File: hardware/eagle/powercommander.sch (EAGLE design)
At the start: 28 parts, among them IC1 ULN2803SO18-1, IC2 7805TV, IC3 MCP2551DIL8, K1 G5NB, K2 G5NB, K3 G5NB, K4 G5NB, K5 G5NB, K6 G5NB, K7 G5NB, K8 G5NB, X2 3KLEMME, X3 2KLEMME, X4 2KLEMME, X5 2KLEMME, X6 2KLEMME

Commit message: neu verkabelt
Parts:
- removed EXT2: EXT2, pinhead:PINHD-2X13
- added D1, D2, D3, D4, D5, D6, D7, D8: (no value), diode:DIODE-SOD323-W
- added D9: (no value), diode:DIODE-MELF-MLL41
- added EXT2-1-4, EXT2-23-26: (no value), pinhead:PINHD-2X2
- added F2: FUSESH35, fuse:FUSESH35
- IC3: value MCP2551DIL8 -> MCP2551SOIC8; device personal-parts:MCP2551DIL8 -> personal-parts:MCP2551SOIC8
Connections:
- net A2 renamed N$14
- net A4 renamed N$9
- net A6 renamed N$12
- net A8 renamed N$13
- removed net N$12 (its old number): IC1.5C, K41.1
- removed net N$13 (its old number): IC1.4C, K51.1
- removed net N$14 (its old number): IC1.3C, K61.1
- removed net N$16: IC1.1C, K81.1
- removed net N$21: EXT1.7, IC1.1B
- removed net N$9 (its old number): IC1.8C, K11.1
- new net N$22: F2.1, PHASE.2
- new net N$24: D8.A, IC1.1C, K81.4
- new net N$26: D6.A, IC1.3C, K61.4
- new net N$27: D5.A, IC1.4C, K51.4
- new net N$28: D4.A, IC1.5C, K41.4
- net +5V: now also D1.C, D2.C, D3.C, D4.C, D5.C, D6.C, D7.C, D8.C, D9.A, EXT2-23-26.4, K11.1, K21.1, K31.1, K41.1, K51.1, K61.1, K71.1, K81.1; no longer EXT2.26, K11.4, K21.4, K31.4, K41.4, K51.4, K61.4, K71.4, K81.4
- net N$10: now also D2.A, K21.4; no longer K21.1
- net N$11: now also D3.A, K31.4; no longer K31.1
- net N$15: now also D7.A, K71.4; no longer K71.1
- net N$2: now also X2.2; no longer X2.1
- net N$20: now also D1.A, IC1.8C, K11.4; no longer EXT1.9, IC1.2B
- net N$5: now also D9.C
- net N$6: now also X2.1; no longer X2.2
- net NULL: now also PHASE.1; no longer PHASE.2
- net PHASE: now also F2.2; no longer PHASE.1
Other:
- moved on the sheet: K1, K2, K3, K4, K5, K6, K7, K8

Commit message: neue board version mit pwm pins
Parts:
- removed EXT2-23-26: (no value), pinhead:PINHD-2X2
- added EXT2-21-26: (no value), pinhead:PINHD-2X3
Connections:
- removed net N$18 (its old number): EXT1.13, IC1.4B
- removed net N$38: EXT1.16, R3.2
- removed net N$39: EXT1.14, R2.2
- removed net N$40: EXT1.12, R1.2
- new net N$16: EXT1.17, IC1.4B
- new net N$21: EXT1.13, IC1.7B
- new net N$25: EXT1.14, IC1.8B
- new net N$29: EXT1.24, R1.2
- new net N$31: EXT1.18, R3.2
- net +5V: now also EXT2-21-26.6; no longer EXT2-23-26.4
- net N$1: now also EXT1.26, IC1.1B; no longer EXT1.21, IC1.8B
- net N$19: now also EXT1.16, IC1.6B; no longer EXT1.11, IC1.3B
- net N$30: now also EXT1.20, R2.2; no longer EXT1.26, IC1.COM
- net N$7: now also EXT1.22, IC1.2B; no longer EXT1.19, IC1.7B
- net N$8: now also EXT1.21, IC1.3B; no longer EXT1.17, IC1.6B
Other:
- moved on the sheet: EXT1, JP3, R1, R2, R3

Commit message: some fixes..
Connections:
- net GND: now also EXT2-21-26.5
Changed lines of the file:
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@@
 <part name="EXT2-21-26" library="pinhead" deviceset="PINHD-2X3" device=""/>
 <part name="EXT2-1-4" library="pinhead" deviceset="PINHD-2X2" device=""/>
+<part name="GND1" library="supply1" deviceset="GND" device=""/>
 </parts>
 <sheets>
@@
 <instance part="EXT2-21-26" gate="A" x="22.86" y="99.06"/>
 <instance part="EXT2-1-4" gate="A" x="25.4" y="83.82"/>
+<instance part="GND1" gate="1" x="10.16" y="91.44"/>
 </instances>
 <busses>
@@
 <wire x1="78.74" y1="139.7" x2="81.28" y2="139.7" width="0.1524" layer="91"/>
 </segment>
-</net>
+<segment>
+<pinref part="EXT2-21-26" gate="A" pin="5"/>
+<pinref part="GND1" gate="1" pin="GND"/>
+<wire x1="20.32" y1="96.52" x2="10.16" y2="96.52" width="0.1524" layer="91"/>
+<wire x1="10.16" y1="96.52" x2="10.16" y2="93.98" width="0.1524" layer="91"/>
+</segment>
+</net>

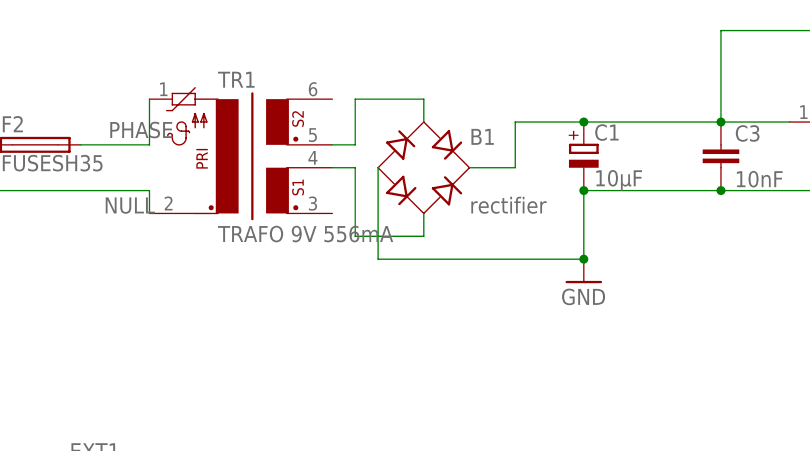
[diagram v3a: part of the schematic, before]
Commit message: removed transformer holes
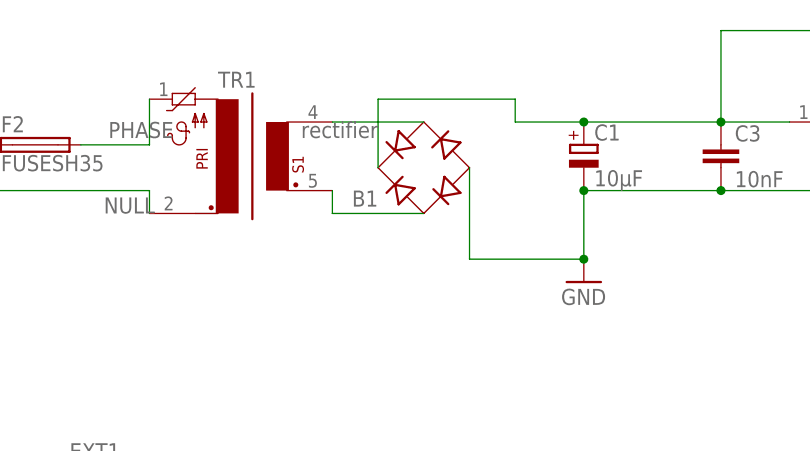
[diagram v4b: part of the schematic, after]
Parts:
- TR1: value TRAFO 9V 556mA -> (none); device trafo:PT04,5-2 -> personal-parts:VC5,0-1
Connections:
- removed net N$3 (its old number): B1.AC1, TR1.5
- new net N$4: B1.AC1, TR1.3
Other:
- moved on the sheet: B1
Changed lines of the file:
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@@
 <part name="IC2" library="linear" deviceset="78*" device="TV" technology="05"/>
 <part name="B1" library="rectifier" deviceset="RB1A" device="" value="rectifier"/>
-<part name="TR1" library="trafo" deviceset="PT04,5-2" device="" value="TRAFO 9V 556mA"/>
 <part name="K1" library="relay-omron-G5NB" deviceset="G5NB" device=""/>
 <part name="C1" library="rcl" deviceset="CPOL-EU" device="E5-8.5" value="10µF"/>
@@
 <part name="EXT2-1-4" library="pinhead" deviceset="PINHD-2X2" device=""/>
 <part name="GND1" library="supply1" deviceset="GND" device=""/>
+<part name="TR1" library="personal-parts" deviceset="VC5,0-1" device=""/>
 </parts>
 <sheets>
@@
 <instance part="X2" gate="G$1" x="147.32" y="76.2"/>
 <instance part="IC2" gate="A1" x="157.48" y="185.42"/>
-<instance part="B1" gate="1" x="106.68" y="180.34"/>
-<instance part="TR1" gate="1" x="86.36" y="182.88"/>
+<instance part="B1" gate="1" x="106.68" y="180.34" rot="R180"/>
 <instance part="K1" gate="1" x="193.04" y="157.48" rot="R270"/>
 <instance part="K1" gate="U" x="287.02" y="165.1"/>
@@
 <instance part="EXT2-1-4" gate="A" x="25.4" y="83.82"/>
 <instance part="GND1" gate="1" x="10.16" y="91.44"/>
+<instance part="TR1" gate="1" x="86.36" y="182.88"/>
 </instances>
 <busses>
@@
 <net name="PHASE" class="0">
 <segment>
-<pinref part="TR1" gate="1" pin="1"/>
 <wire x1="76.2" y1="182.88" x2="76.2" y2="187.96" width="0.1524" layer="91"/>
 <label x="71.628" y="183.642" size="1.778" layer="95"/>
 <pinref part="F2" gate="G$1" pin="2"/>
 <wire x1="68.58" y1="182.88" x2="76.2" y2="182.88" width="0.1524" layer="91"/>
+<pinref part="TR1" gate="1" pin="1"/>
 </segment>
 <segment>
@@
 <net name="NULL" class="0">
 <segment>
-<pinref part="TR1" gate="1" pin="2"/>
 <wire x1="76.2" y1="177.8" x2="76.2" y2="175.26" width="0.1524" layer="91"/>
 <label x="71.12" y="175.26" size="1.778" layer="95"/>
 <pinref part="PHASE" gate="G$1" pin="1"/>
 <wire x1="76.2" y1="177.8" x2="53.34" y2="177.8" width="0.1524" layer="91"/>
-</segment>
-</net>
-<net name="N$3" class="0">
-<segment>
-<pinref part="TR1" gate="1" pin="5"/>
-<wire x1="96.52" y1="182.88" x2="99.06" y2="182.88" width="0.1524" layer="91"/>
-<wire x1="99.06" y1="182.88" x2="99.06" y2="187.96" width="0.1524" layer="91"/>
-<pinref part="B1" gate="1" pin="AC1"/>
-<wire x1="99.06" y1="187.96" x2="106.68" y2="187.96" width="0.1524" layer="91"/>
-<wire x1="106.68" y1="187.96" x2="106.68" y2="185.42" width="0.1524" layer="91"/>
-</segment>
-</net>
-<net name="N$4" class="0">
-<segment>
-<pinref part="TR1" gate="1" pin="4"/>
-<wire x1="96.52" y1="180.34" x2="99.06" y2="180.34" width="0.1524" layer="91"/>
-<wire x1="99.06" y1="180.34" x2="99.06" y2="172.72" width="0.1524" layer="91"/>
-<pinref part="B1" gate="1" pin="AC2"/>
-<wire x1="99.06" y1="172.72" x2="106.68" y2="172.72" width="0.1524" layer="91"/>
-<wire x1="106.68" y1="172.72" x2="106.68" y2="175.26" width="0.1524" layer="91"/>
+<pinref part="TR1" gate="1" pin="2"/>
 </segment>
 </net>
@@
 <segment>
 <pinref part="B1" gate="1" pin="+"/>
-<wire x1="111.76" y1="180.34" x2="116.84" y2="180.34" width="0.1524" layer="91"/>
-<wire x1="116.84" y1="180.34" x2="116.84" y2="185.42" width="0.1524" layer="91"/>
+<wire x1="101.6" y1="180.34" x2="101.6" y2="187.96" width="0.1524" layer="91"/>
+<wire x1="101.6" y1="187.96" x2="116.84" y2="187.96" width="0.1524" layer="91"/>
+<wire x1="116.84" y1="187.96" x2="116.84" y2="185.42" width="0.1524" layer="91"/>
 <pinref part="C1" gate="G$1" pin="+"/>
 <wire x1="116.84" y1="185.42" x2="124.46" y2="185.42" width="0.1524" layer="91"/>
@@
 <segment>
 <pinref part="B1" gate="1" pin="-"/>
-<wire x1="101.6" y1="180.34" x2="101.6" y2="170.18" width="0.1524" layer="91"/>
+<wire x1="111.76" y1="180.34" x2="111.76" y2="170.18" width="0.1524" layer="91"/>
 <pinref part="C1" gate="G$1" pin="-"/>
-<wire x1="101.6" y1="170.18" x2="124.46" y2="170.18" width="0.1524" layer="91"/>
+<wire x1="111.76" y1="170.18" x2="124.46" y2="170.18" width="0.1524" layer="91"/>
 <wire x1="124.46" y1="170.18" x2="124.46" y2="177.8" width="0.1524" layer="91"/>
 <pinref part="C3" gate="G$1" pin="2"/>
@@
 </segment>
 </net>
+<net name="N$3" class="0">
+<segment>
+<pinref part="TR1" gate="1" pin="4"/>
+<pinref part="B1" gate="1" pin="AC2"/>
+<wire x1="96.52" y1="185.42" x2="106.68" y2="185.42" width="0.1524" layer="91"/>
+</segment>
+</net>
+<net name="N$4" class="0">
+<segment>
+<pinref part="TR1" gate="1" pin="3"/>
+<pinref part="B1" gate="1" pin="AC1"/>
+<wire x1="96.52" y1="177.8" x2="96.52" y2="175.26" width="0.1524" layer="91"/>
+<wire x1="96.52" y1="175.26" x2="106.68" y2="175.26" width="0.1524" layer="91"/>
+</segment>
+</net>

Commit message: board and schematic fancyfied
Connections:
- net N$1 renamed 1B
- net N$16 renamed 4B
- net N$17 renamed 5B
- net N$18 renamed CAN_RX
- net N$19 renamed 6B
- net N$21 renamed 7B
- net N$22 renamed L
- net N$23 renamed CAN_TX
- net N$25 renamed 8B
- net N$29 renamed LED1
- net N$30 renamed LED2
- net N$31 renamed LED3
- net N$7 renamed 2B
- net N$8 renamed 3B
- net PHASE renamed L_FUSE
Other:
- note removed: "Kann noch umgelegt werden"
- moved on the sheet: B1, C1, C2, C3, D1, D2, D3, D4, D5, D6, D7, D8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

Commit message: klemme angepasst
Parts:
- D1, D2, D3, D4, D5, D6, D7, D8: value (none) -> 1N4148
- D9: value (none) -> 1N4001
- EXT2-1-4: value (none) -> 2x2
- EXT2-21-26: value (none) -> 3x2
- TR1: value (none) -> VC5,0-1
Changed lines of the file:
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@@
 <setting verticaltext="up"/>
 </settings>
-<grid distance="0.1" unitdist="inch" unit="inch" style="lines" multiple="1" display="no" altdistance="0.025" altunitdist="inch" altunit="inch"/>
+<grid distance="0.1" unitdist="inch" unit="inch" style="lines" multiple="1" display="no" altdistance="0.01" altunitdist="inch" altunit="inch"/>
 <layers>
 <layer number="1" name="Top" color="4" fill="1" visible="no" active="no"/>
@@
 </classes>
 <parts>
-<part name="FRAME1" library="frames" deviceset="A3L-LOC" device=""/>
 <part name="EXT1" library="pinhead" deviceset="PINHD-2X13" device="" value="EXT1"/>
 <part name="IC1" library="personal-parts" deviceset="ULN2803" device="SO18-1"/>
@@
 <part name="P+4" library="supply1" deviceset="+5V" device=""/>
 <part name="F2" library="fuse" deviceset="FUSE" device="SH35"/>
-<part name="D1" library="diode" deviceset="DIODE-" device="SOD323-W"/>
-<part name="D2" library="diode" deviceset="DIODE-" device="SOD323-W"/>
-<part name="D3" library="diode" deviceset="DIODE-" device="SOD323-W"/>
-<part name="D4" library="diode" deviceset="DIODE-" device="SOD323-W"/>
-<part name="D5" library="diode" deviceset="DIODE-" device="SOD323-W"/>
-<part name="D6" library="diode" deviceset="DIODE-" device="SOD323-W"/>
-<part name="D7" library="diode" deviceset="DIODE-" device="SOD323-W"/>
-<part name="D8" library="diode" deviceset="DIODE-" device="SOD323-W"/>
-<part name="D9" library="diode" deviceset="DIODE-" device="MELF-MLL41"/>
-<part name="EXT2-21-26" library="pinhead" deviceset="PINHD-2X3" device=""/>
-<part name="EXT2-1-4" library="pinhead" deviceset="PINHD-2X2" device=""/>
+<part name="D1" library="diode" deviceset="DIODE-" device="SOD323-W" value="1N4148"/>
+<part name="D2" library="diode" deviceset="DIODE-" device="SOD323-W" value="1N4148"/>
+<part name="D3" library="diode" deviceset="DIODE-" device="SOD323-W" value="1N4148"/>
+<part name="D4" library="diode" deviceset="DIODE-" device="SOD323-W" value="1N4148"/>
+<part name="D5" library="diode" deviceset="DIODE-" device="SOD323-W" value="1N4148"/>
+<part name="D6" library="diode" deviceset="DIODE-" device="SOD323-W" value="1N4148"/>
+<part name="D7" library="diode" deviceset="DIODE-" device="SOD323-W" value="1N4148"/>
+<part name="D8" library="diode" deviceset="DIODE-" device="SOD323-W" value="1N4148"/>
+<part name="D9" library="diode" deviceset="DIODE-" device="MELF-MLL41" value="1N4001"/>
+<part name="EXT2-21-26" library="pinhead" deviceset="PINHD-2X3" device="" value="3x2"/>
+<part name="EXT2-1-4" library="pinhead" deviceset="PINHD-2X2" device="" value="2x2"/>
 <part name="GND1" library="supply1" deviceset="GND" device=""/>
-<part name="TR1" library="personal-parts" deviceset="VC5,0-1" device=""/>
-<part name="FRAME2" library="frames" deviceset="DINA4_L" device=""/>
+<part name="TR1" library="personal-parts" deviceset="VC5,0-1" device="" value="VC5,0-1"/>
+<part name="FRAME2" library="frames" deviceset="DINA4_L" device="" value="01"/>
 </parts>
 <sheets>
@@
 </plain>
 <instances>
-<instance part="FRAME1" gate="G$1" x="195.58" y="266.7"/>
 <instance part="EXT1" gate="A" x="60.96" y="152.4"/>
 <instance part="IC1" gate="&gt;NAME" x="132.08" y="147.32" rot="MR180"/>

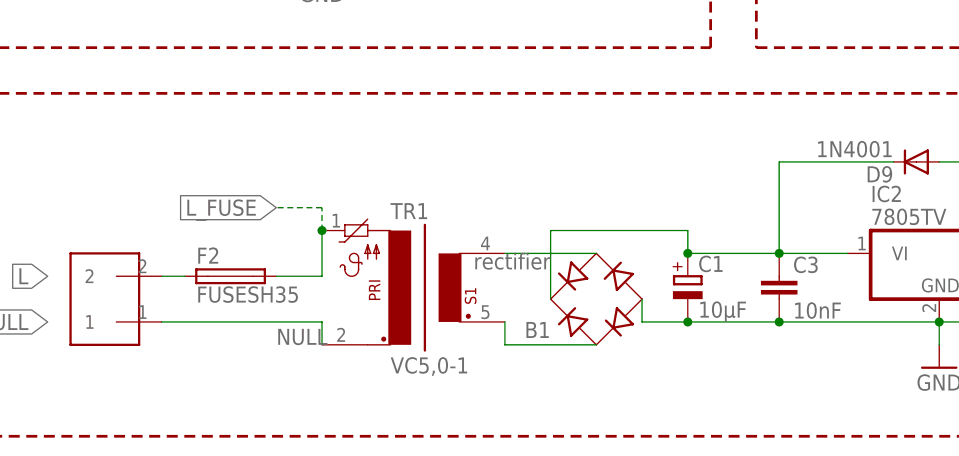
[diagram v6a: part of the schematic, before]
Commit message: new boardlayout +  pwm  für relay added
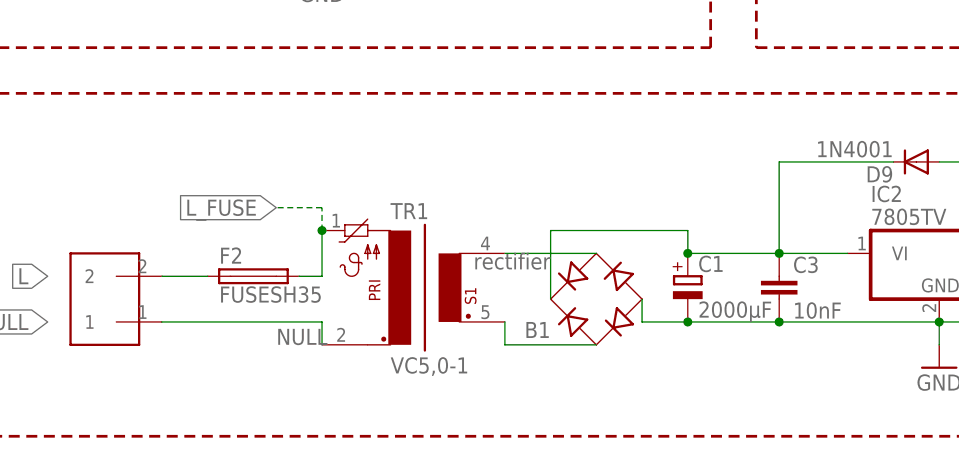
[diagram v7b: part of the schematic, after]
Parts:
- C1: value 10µF -> 2000µF
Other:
- moved on the sheet: F2
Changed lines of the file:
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@@
 <part name="B1" library="rectifier" deviceset="RB1A" device="" value="rectifier"/>
 <part name="K1" library="relay-omron-G5NB" deviceset="G5NB" device=""/>
-<part name="C1" library="rcl" deviceset="CPOL-EU" device="E5-8.5" value="10µF"/>
+<part name="C1" library="rcl" deviceset="CPOL-EU" device="E5-8.5" value="2000µF"/>
 <part name="C2" library="rcl" deviceset="CPOL-EU" device="E5-8.5" value="10µF"/>
 <part name="C3" library="rcl" deviceset="C-EU" device="025-025X050" value="10nF"/>
@@
 <instance part="GND8" gate="1" x="50.8" y="55.88"/>
 <instance part="P+4" gate="1" x="187.96" y="154.94" rot="R270"/>
-<instance part="F2" gate="G$1" x="40.64" y="22.86"/>
+<instance part="F2" gate="G$1" x="43.18" y="22.86"/>
 <instance part="D1" gate="G$1" x="170.18" y="160.655"/>
 <instance part="D2" gate="G$1" x="170.18" y="147.955"/>
@@
 <wire x1="50.8" y1="22.86" x2="50.8" y2="27.94" width="0.1524" layer="91"/>
 <pinref part="F2" gate="G$1" pin="2"/>
-<wire x1="45.72" y1="22.86" x2="50.8" y2="22.86" width="0.1524" layer="91"/>
+<wire x1="48.26" y1="22.86" x2="50.8" y2="22.86" width="0.1524" layer="91"/>
 <pinref part="TR1" gate="1" pin="1"/>
 <label x="45.72" y="30.48" size="1.778" layer="95" rot="R180" xref="yes"/>
@@
 <pinref part="F2" gate="G$1" pin="1"/>
 <pinref part="PHASE" gate="G$1" pin="2"/>
-<wire x1="35.56" y1="22.86" x2="33.02" y2="22.86" width="0.1524" layer="91"/>
+<wire x1="38.1" y1="22.86" x2="33.02" y2="22.86" width="0.1524" layer="91"/>
 <label x="20.32" y="22.86" size="1.778" layer="95" rot="R180" xref="yes"/>
 </segment>
